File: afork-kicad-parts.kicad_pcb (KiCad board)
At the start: 2 copper layers, 9 parts, among them J5 Tinker-USB_C, U11 SRV05-4, U2 ATMEGA168A-AU, U3 ESP32-S3-WROOM-1, U4 LMR38020, U7 MP2451, U8 NE555P, X1 MHz

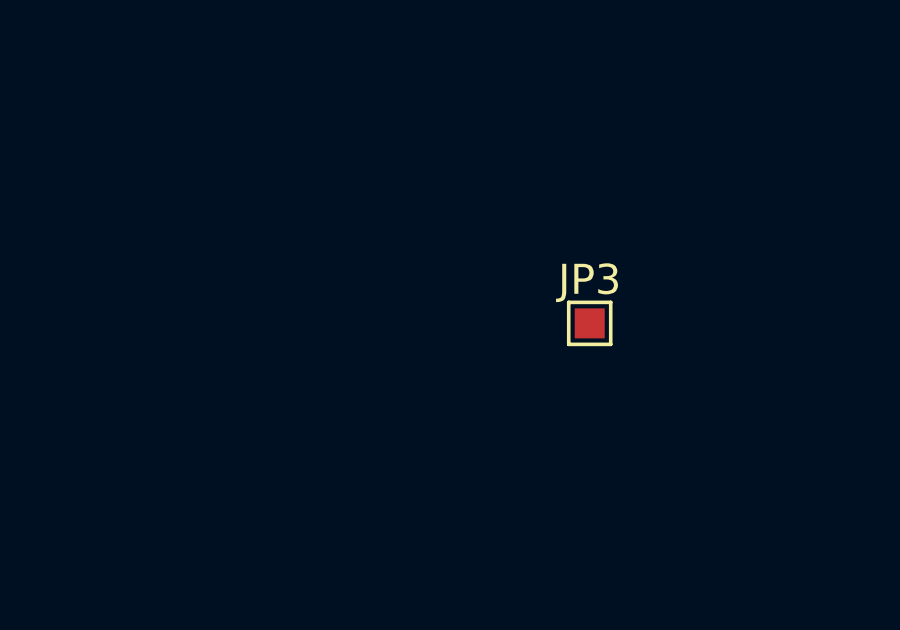
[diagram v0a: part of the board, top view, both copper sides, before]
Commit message: Clean up jumpers to allow mine and Tinker's.
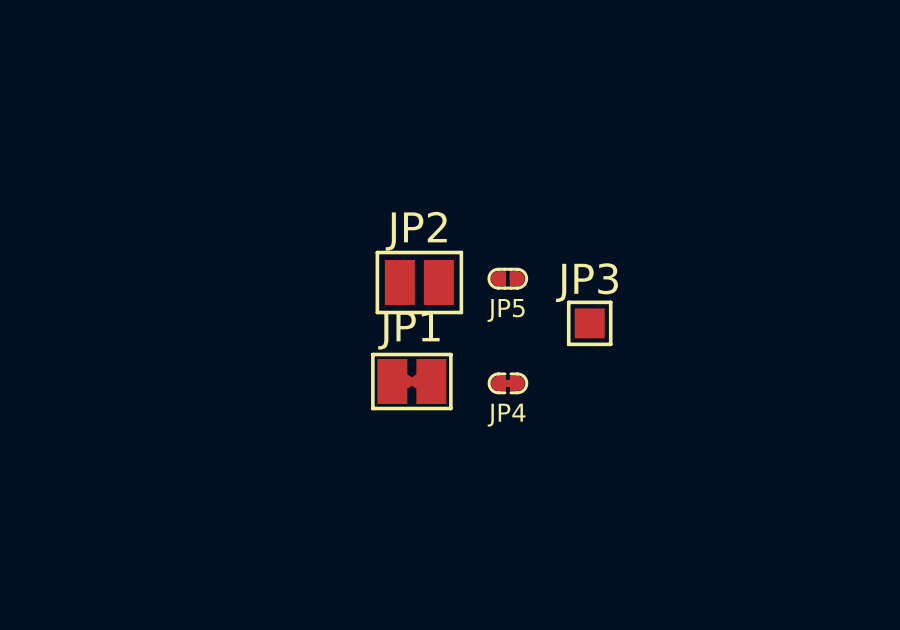
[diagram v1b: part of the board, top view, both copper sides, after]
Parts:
- added JP1: PCB_Patch, afork-kicad-parts:SolderJumper-2_P1.3mm_Bridged_Pad1.0x1.5mm, F.Cu at (153.4, 79.9)
- added JP2: PCB_Patch-open, afork-kicad-parts:SolderJumper-2_P1.3mm_Open_Pad1.0x1.5mm, F.Cu at (153.6, 76.6)
- added JP4: PCB_Patch, afork-kicad-parts:tinySJ-Bridged, F.Cu at (156.6, 79.9)
- added JP5: PCB_Patch-open, afork-kicad-parts:tinySJ-Open, F.Cu at (156.6, 76.4)
